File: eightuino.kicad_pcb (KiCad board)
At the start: 2 copper layers, 49.5 x 49.5 mm, 27 parts, among them CON1 BARREL_JACK, CON2 ISP, IC1 ATMEGA8-P, P1 PowerPins, P2 Analog, P3 Digital1, P4 Digital_2, SW1 Reset, U1 1117-33, X1 CRYSTAL

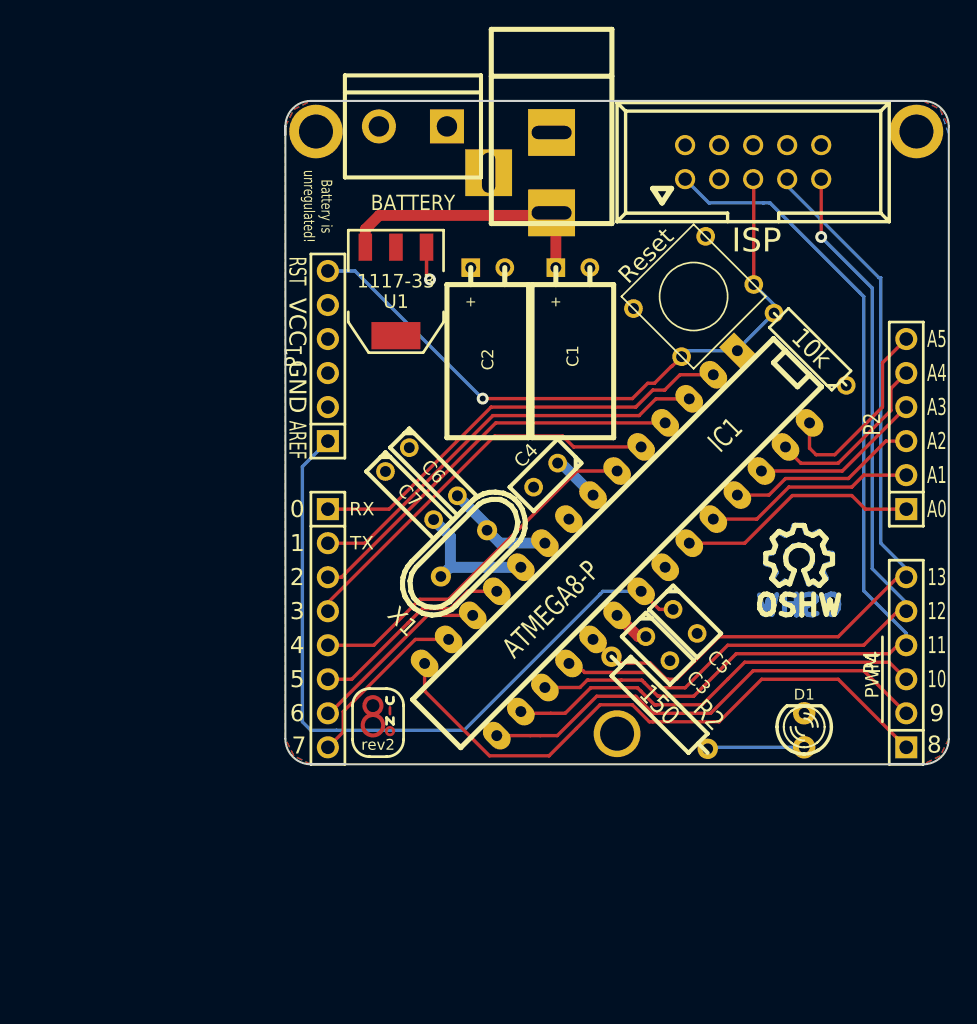
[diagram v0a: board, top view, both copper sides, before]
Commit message: Almost total board rework.
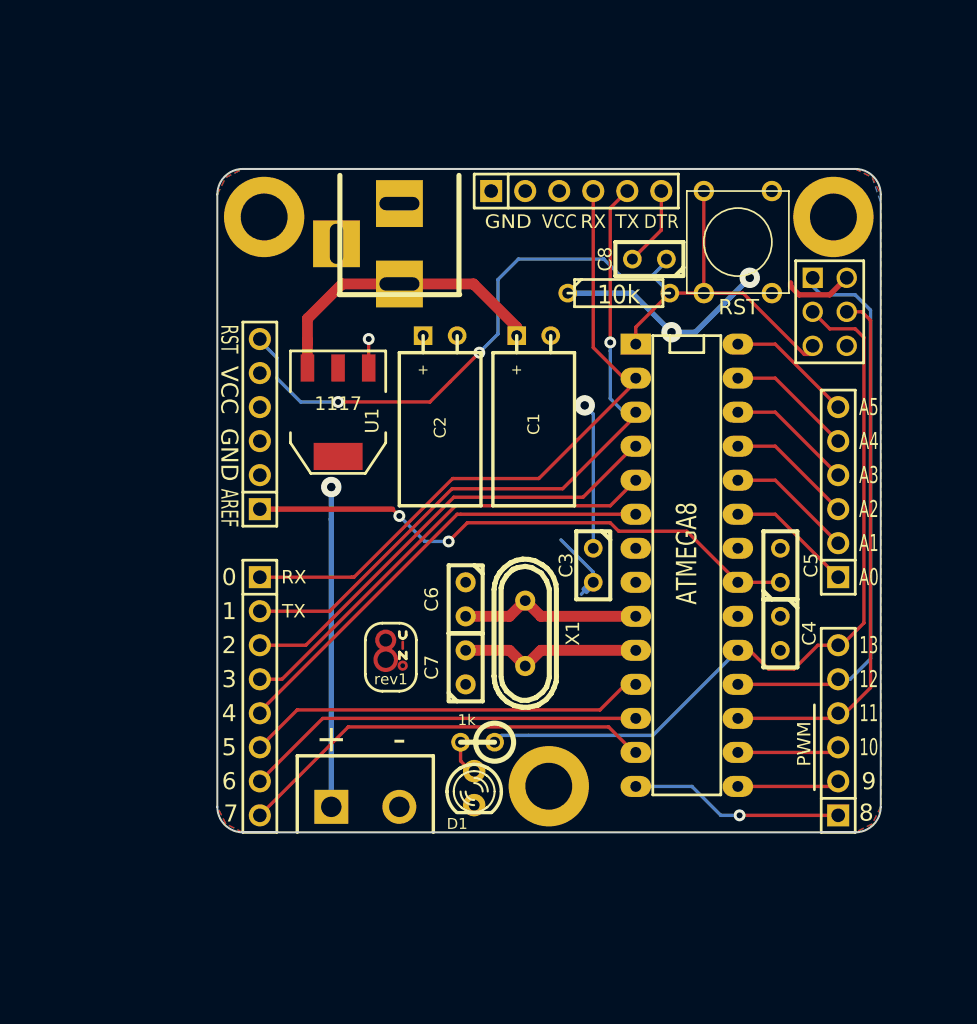
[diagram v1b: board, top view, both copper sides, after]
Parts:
- removed CON2: ISP, Connect:VASCH5x2
- removed the SYM at (164.0, 108.1)
- added C8: 100nF, Discret:C1, F.Cu at (152.8, 85.7)
- added P5: Serial, pinheaders:Pinrow_6p, F.Cu at (147.3, 80.6)
- added P6: ISP, Pin_Arrays:pin_array_3x2, F.Cu at (166.2, 89.7)
- 8uino2: value rev2 -> rev1; footprint 8uino_mix_mask+cupper -> 8uino_mix_silk+mask+copper
- BT1: value BATTERY -> Unregulated Battery
- C6, C7: footprint Discret:C2 -> Capacitors:cnp_3mm_disc
- IC1: value ATMEGA8-P -> ATMEGA8
- R2: value 150 -> 1k; footprint Discret:R4 -> Discret:R1
- SW1: value Reset -> RST
- SYM: moved to B.Cu
- U1: value 1117-33 -> 1117
- moved BT1 50.9 mm to (131.6, 126.6), turned to 0 degrees
- moved SYM 29.1 mm to (135.4, 113.6), turned to 90 degrees
- moved D1 25.0 mm to (139.7, 125.2), turned to 270 degrees
- moved C4 21.1 mm to (162.6, 113.7), turned to 270 degrees
- moved R1 14.9 mm to (150.5, 88.3), turned to 0 degrees
- moved R2 13.9 mm to (140.0, 121.8), turned to 180 degrees
- moved C7 13.5 mm to (139.1, 116.2), turned to 90 degrees
- moved CON1 12.5 mm to (134.1, 81.4)
- moved U1 10.00 mm to (129.5, 97.2)
- moved C6 9.83 mm to (139.1, 111.1), turned to 270 degrees
- moved 1PIN 8.90 mm to (166.5, 82.6)
- moved C5 8.25 mm to (162.6, 108.6), turned to 90 degrees
- moved C3 7.88 mm to (148.6, 108.6), turned to 270 degrees
- moved X1 7.52 mm to (143.5, 113.7), turned to 90 degrees
- moved 1PIN 7.46 mm to (124.0, 82.6)
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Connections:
- net Net-(CON2-Pad1) renamed /MOSI
- net Net-(CON2-Pad5) renamed /RST
- net Net-(CON2-Pad7) renamed /SCK
- net Net-(CON2-Pad9) renamed /MISO
- net Net-(IC1-Pad2) renamed /RX
- net Net-(IC1-Pad3) renamed /TX
- 1PIN pad 1: (no net) -> GND (x3)
- P3 pad 7: (no net) -> Net-(IC1-Pad12)
- P3 pad 8: (no net) -> Net-(IC1-Pad13)
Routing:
- net VCC: track 6.44 -> 56.8 mm, vias 0 -> 4
- net /MOSI: track 73.6 -> 40.3 mm
- net Net-(IC1-Pad14): track 45.5 -> 16.0 mm, vias 0 -> 1
- net Net-(IC1-Pad15): track 34.9 -> 7.65 mm
- net Net-(IC1-Pad16): track 32.0 -> 7.65 mm
- net /MISO: track 63.1 -> 41.8 mm, vias 1 -> 0
- net /TX: track 31.4 -> 52.7 mm, vias 0 -> 1
- net Net-(IC1-Pad13): track 13.2 -> 31.6 mm
- net /RST: track 50.6 -> 68.2 mm, vias 1 -> 2
- net /RX: track 32.9 -> 50.2 mm
- net Net-(IC1-Pad12): track 13.8 -> 30.0 mm
- net Net-(IC1-Pad11): track 15.3 -> 30.0 mm
- net Net-(C5-Pad1): track 54.5 -> 42.3 mm, vias 0 -> 2
- net Net-(IC1-Pad23): track 18.1 -> 9.44 mm
- net Net-(IC1-Pad6): track 27.0 -> 34.3 mm
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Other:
- outline, holes or cut-outs redrawn
- net class 0,016 added: clearance 0.254, trace_width 0.4064, via_dia 1.524, via_drill 1.016
- net class 0.032: via_dia 0.889 -> 1.524; via_drill 0.635 -> 1.016
- net class Default: clearance 0.254 -> 0.2413
- rule trace_clearance: 0.254 -> 0.2413
- board text added: "DTR"
- board text added: "Eightuino rev1 © 2013 Niels Kjøller Hansen lab.kjlr.dk/p/eightuino"
- board text added: "Recommended: C1: 10uF C2: 47uF C3,C4,C5,C8: 100nF Optional: X1: 16MHz C6,C7: 22pF"
- board text removed: "Battery is unregulated!"
- board text removed: "Eightuino rev2 © 2013 Niels Kjøller Hansen lab.kjlr.dk/projects/eightuino"
- board text removed: "Recommended: C1: 10uF C2: 47uF C3,C4,C5: 100nF Optional: X1: 16MHz C6,C7: 22pF Replace Atmega8L"

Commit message: Components mostly laid out, tracks still missing
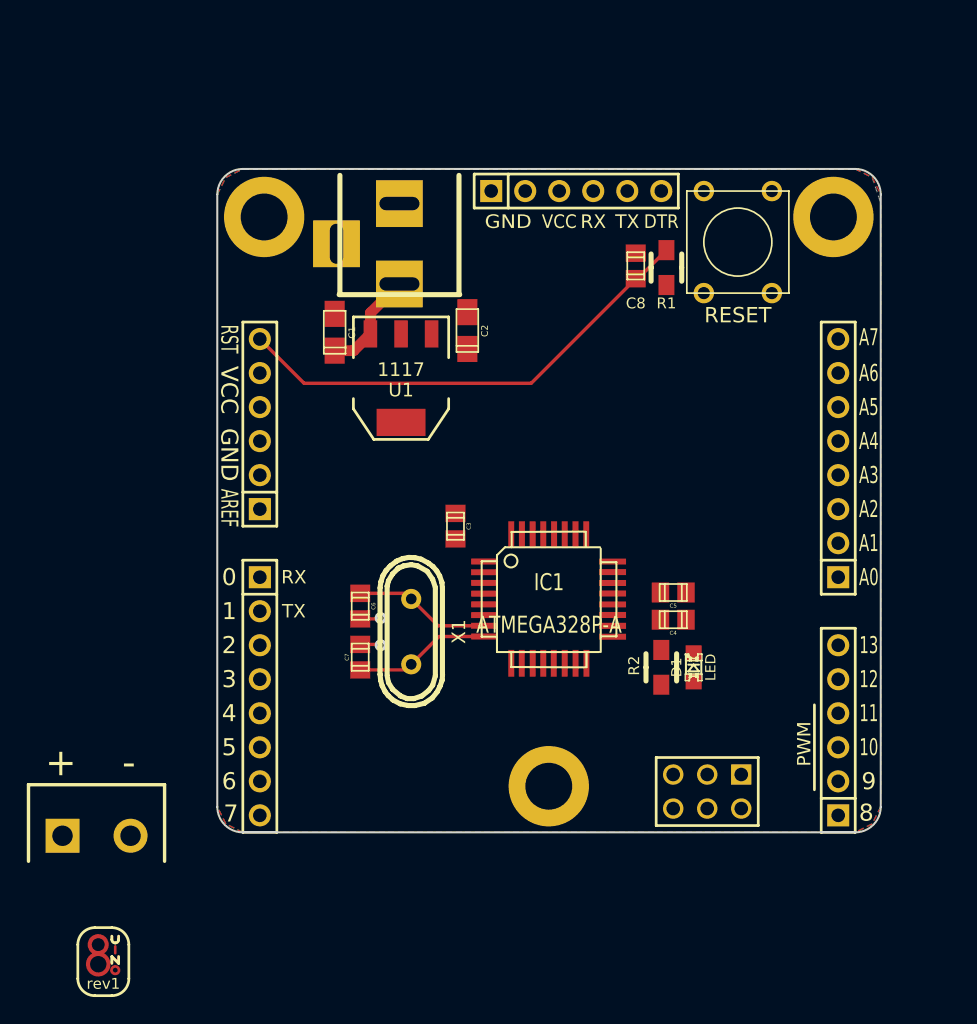
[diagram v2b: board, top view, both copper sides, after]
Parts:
- BT1: value Unregulated Battery -> BATTERY
- C1, C2: footprint Discret:C1V5H -> Capacitors_SMD:c_tant_A
- C3, C4, C5, C8: footprint Discret:C1 -> Capacitors_SMD:c_0805
- C6, C7: footprint Capacitors:cnp_3mm_disc -> Capacitors_SMD:c_0805
- D1: footprint LEDs:LED-3MM -> LEDs:LED-0805
- IC1: value ATMEGA8 -> ATMEGA328P-A; footprint Sockets_DIP:DIP-28__300_ELL -> SMD_Packages:TQFP32
- P2: footprint Pinheaders:Pinrow_6p -> pinheaders:Pinrow_8p
- R1: footprint Discret:R3 -> Resistors_SMD:Resistor_SMD0805_HandSoldering_RevA_Date21Jun2010
- R2: value 1k -> 150; footprint Discret:R1 -> Resistors_SMD:Resistor_SMD0805_HandSoldering_RevA_Date21Jun2010
- SW1: value RST -> RESET
- moved P6 37.0 mm to (157.1, 125.5), turned to 180 degrees
- moved 8uino2 31.3 mm to (112.0, 138.8)
- moved SYM 31.3 mm to (114.0, 136.3)
- moved BT1 20.2 mm to (111.5, 128.8)
- moved D1 18.7 mm to (156.1, 116.2), turned to 90 degrees
- moved C1 14.9 mm to (129.3, 91.2), turned to 270 degrees
- moved R2 14.8 mm to (153.7, 116.2), turned to 270 degrees
- moved C3 10.7 mm to (138.3, 105.7)
- moved IC1 10.6 mm to (145.3, 111.1), turned to 0 degrees
- moved X1 8.51 mm to (135.0, 113.5)
- moved C5 8.26 mm to (154.6, 110.6), turned to 180 degrees
- moved C4 8.07 mm to (154.6, 112.6), turned to 180 degrees
- moved C7 7.91 mm to (131.2, 115.4)
- moved C6 7.89 mm to (131.2, 111.6)
- moved U1 5.34 mm to (134.2, 94.6)
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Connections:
- IC1 pad 1: /RST -> Net-(IC1-Pad1)
- IC1 pad 10: /XTAL2 -> Net-(IC1-Pad10)
- IC1 pad 15: Net-(IC1-Pad15) -> /MOSI
- IC1 pad 16: Net-(IC1-Pad16) -> /MISO
- IC1 pad 17: /MOSI -> /SCK
- IC1 pad 18: /MISO -> VCC
- IC1 pad 19: /SCK -> /ADC6
- IC1 pad 2: /RX -> Net-(IC1-Pad2)
- IC1 pad 20: VCC -> Net-(C5-Pad1)
- IC1 pad 21: Net-(C5-Pad1) -> Net-(IC1-Pad21)
- IC1 pad 22: GND -> /ADC7
- IC1 pad 3: /TX -> Net-(IC1-Pad3)
- IC1 pad 4: Net-(IC1-Pad4) -> VCC
- IC1 pad 6: Net-(IC1-Pad6) -> VCC
- IC1 pad 7: VCC -> /XTAL1
- IC1 pad 8: GND -> /XTAL2
- IC1 pad 9: /XTAL1 -> Net-(IC1-Pad9)
- P3 pad 3: Net-(IC1-Pad4) -> Net-(IC1-Pad32)
- P3 pad 4: Net-(IC1-Pad5) -> Net-(IC1-Pad1)
- P3 pad 5: Net-(IC1-Pad6) -> Net-(IC1-Pad2)
- P3 pad 6: Net-(IC1-Pad11) -> Net-(IC1-Pad9)
- P3 pad 7: Net-(IC1-Pad12) -> Net-(IC1-Pad10)
- P3 pad 8: Net-(IC1-Pad13) -> Net-(IC1-Pad11)
- P4 pad 1: Net-(IC1-Pad14) -> Net-(IC1-Pad12)
- P4 pad 2: Net-(IC1-Pad15) -> Net-(IC1-Pad13)
- P4 pad 3: Net-(IC1-Pad16) -> Net-(IC1-Pad14)
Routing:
- net /SCK: track 58.3 -> 0.00 mm
- net VCC: track 56.8 -> 0.00 mm, vias 4 -> 0
- net /TX: track 52.7 -> 0.00 mm, vias 1 -> 0
- net /RX: track 50.2 -> 0.00 mm
- net Net-(C5-Pad1): track 42.3 -> 0.00 mm, vias 2 -> 0
- net /MISO: track 41.8 -> 0.00 mm
- net /MOSI: track 40.3 -> 0.00 mm
- net Net-(IC1-Pad6): track 34.3 -> 0.00 mm
- net Net-(IC1-Pad5): track 34.2 -> 0.00 mm
- net Net-(IC1-Pad4): track 34.2 -> 0.00 mm
- net /RST: track 68.2 -> 35.8 mm, vias 2 -> 0
- net Net-(IC1-Pad13): track 31.6 -> 0.00 mm
- net Net-(IC1-Pad11): track 30.0 -> 0.00 mm
- net Net-(IC1-Pad12): track 30.0 -> 0.00 mm
- net Net-(IC1-Pad14): track 16.0 -> 0.00 mm, vias 1 -> 0
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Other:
- board text added: "A6"
- board text added: "A7"
